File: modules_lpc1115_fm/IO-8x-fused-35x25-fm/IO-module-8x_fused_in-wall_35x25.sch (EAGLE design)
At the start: 82 parts, among them IC1 LPC1115, IC2 ATAES132A-SHEQ-T, Q2 ASFL, U1 EEPROM, X3 MICROMATCH-10

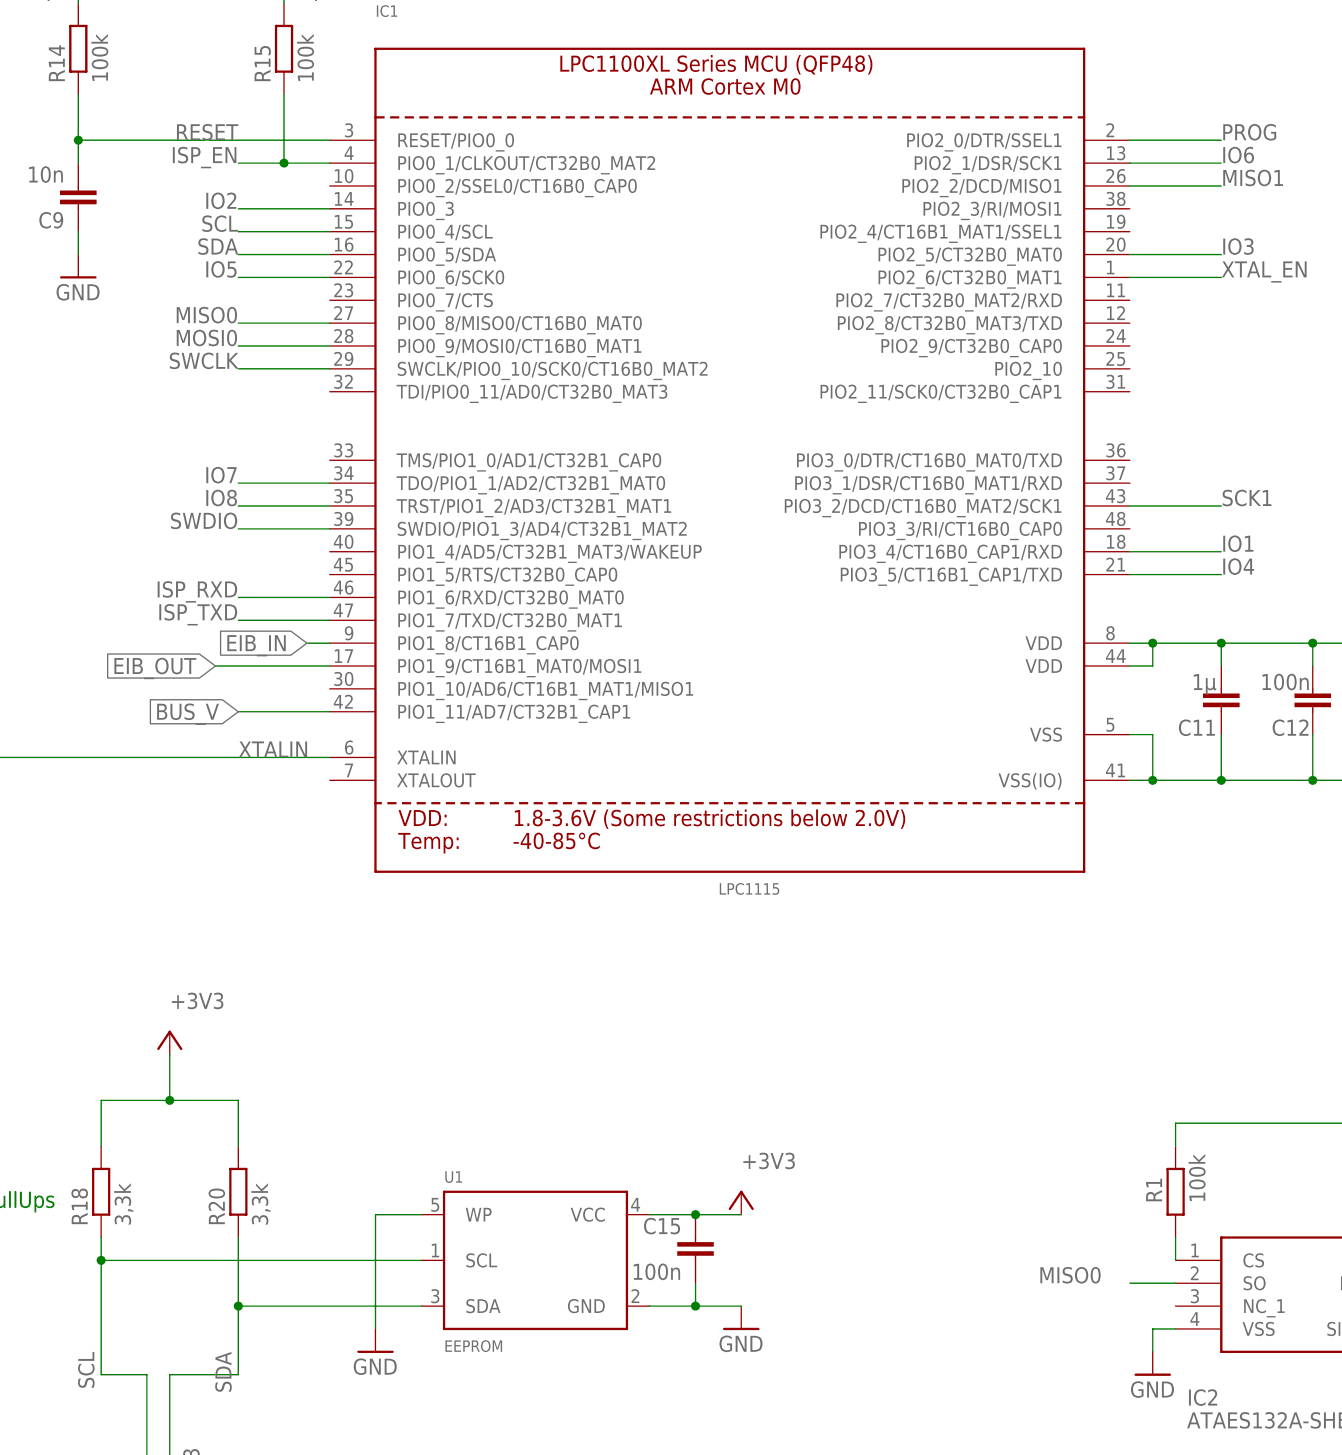
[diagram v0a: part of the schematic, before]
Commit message: [IOmodule8xUP]  added SPI footprint to SSEL0
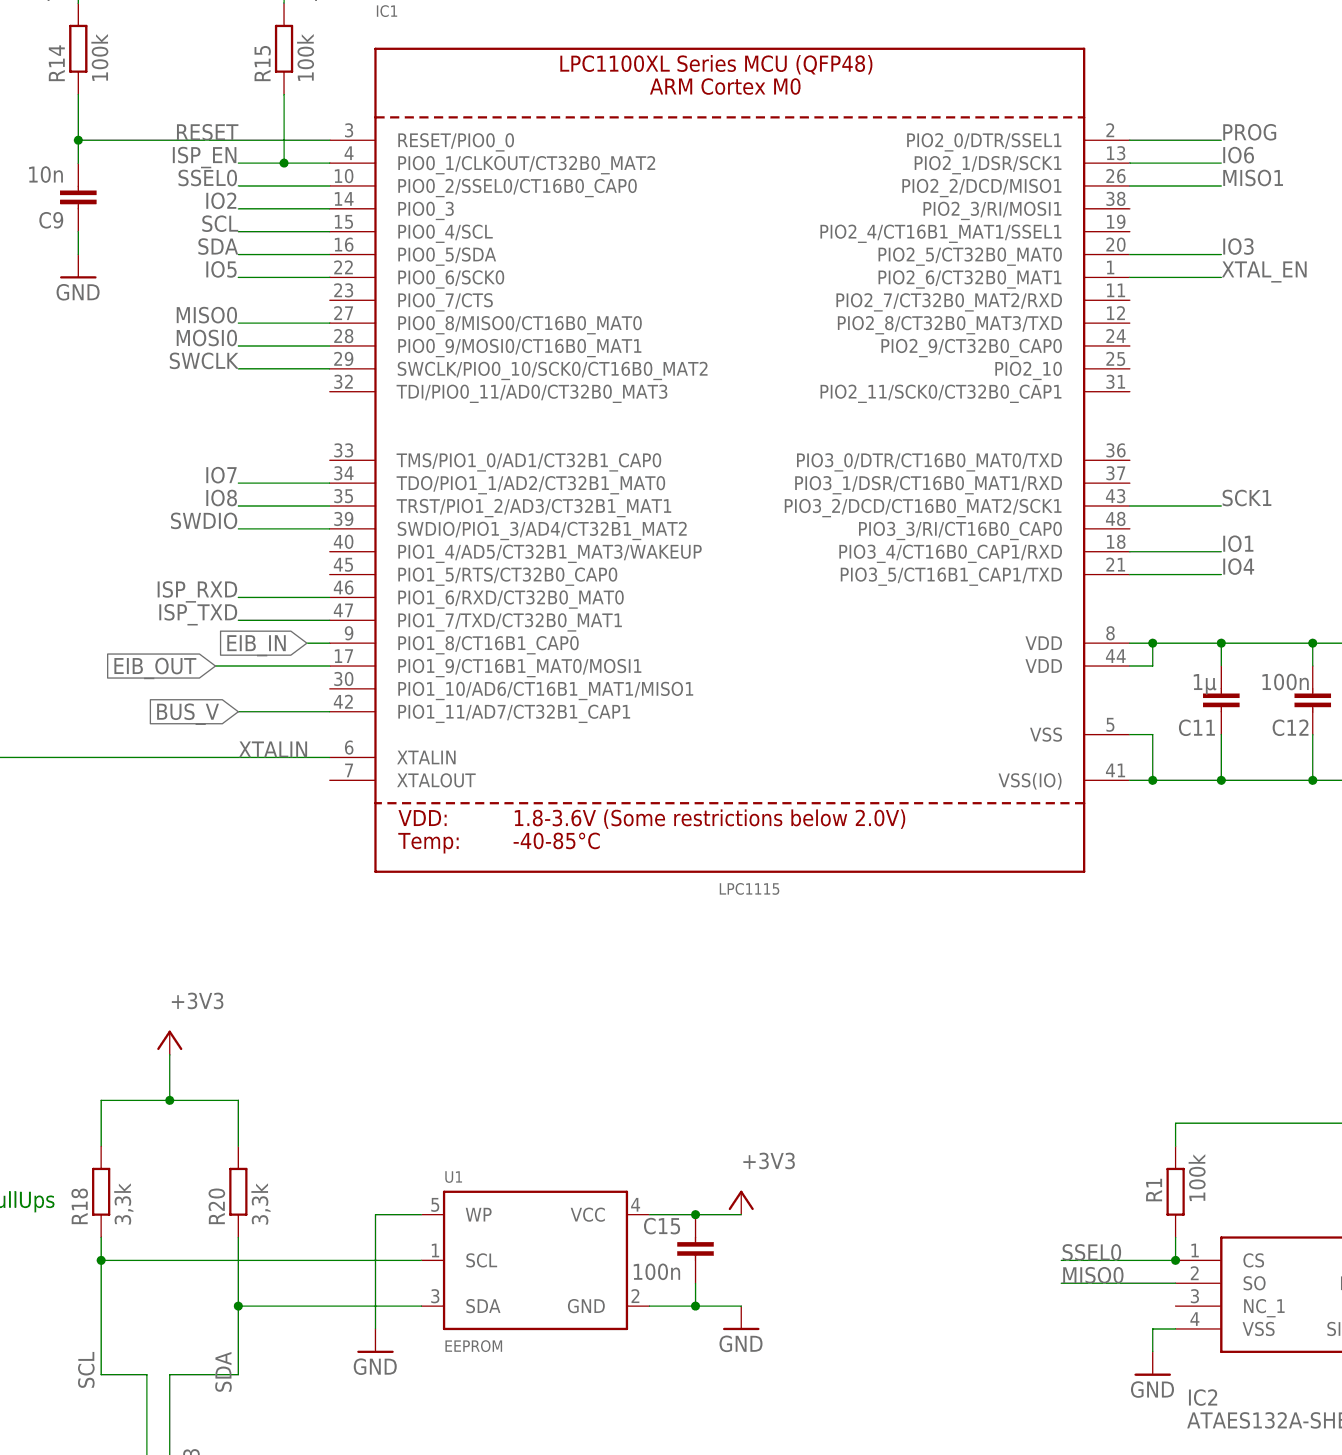
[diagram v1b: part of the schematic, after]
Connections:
- removed net N$19: IC2.CS, R1.1
- new net SSEL0: IC1.PIO0_2/SSEL0/CT16B0_CAP0, IC2.CS, R1.1
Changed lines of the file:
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@@
 <segment>
 <pinref part="IC2" gate="G$1" pin="SO"/>
-<wire x1="411.48" y1="45.72" x2="406.4" y2="45.72" width="0.1524" layer="91"/>
-<label x="396.24" y="45.72" size="1.778" layer="95"/>
+<label x="398.78" y="45.72" size="1.778" layer="95"/>
+<wire x1="411.48" y1="45.72" x2="398.78" y2="45.72" width="0.1524" layer="91"/>
 </segment>
 </net>
@@
 </segment>
 </net>
-<net name="N$19" class="0">
+<net name="SSEL0" class="0">
 <segment>
 <pinref part="IC2" gate="G$1" pin="CS"/>
 <pinref part="R1" gate="G$1" pin="1"/>
 <wire x1="411.48" y1="48.26" x2="411.48" y2="50.8" width="0.1524" layer="91"/>
+<junction x="411.48" y="48.26"/>
+<wire x1="411.48" y1="48.26" x2="398.78" y2="48.26" width="0.1524" layer="91"/>
+<label x="398.78" y="48.26" size="1.778" layer="95"/>
+</segment>
+<segment>
+<pinref part="IC1" gate="G$1" pin="PIO0_2/SSEL0/CT16B0_CAP0"/>
+<wire x1="317.5" y1="167.64" x2="307.34" y2="167.64" width="0.1524" layer="91"/>
+<label x="307.34" y="167.64" size="1.778" layer="95" align="bottom-right"/>
 </segment>
 </net>
@@
 for full support of SPICE simulation.
 </note>
+<note version="9.0" severity="warning">
+Since Version 9.0, EAGLE supports the align property for labels.
+Labels in schematic will not be understood with this version. Update EAGLE to the latest version
+for full support of labels.
+</note>
 </compatibility>
